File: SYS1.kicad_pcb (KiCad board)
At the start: 2 copper layers, 111 parts, among them J1 Conn_02x08_Counter_Clockwise_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, J101 Conn_01x03_Pin, J2 Micro_SD_Card, J3 SIM8051-6-0-14-01-X-REVD, J4 Conn_01x04_Pin, J5 Conn_02x08_Counter_Clockwise_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, J6 2169890001, Q1 NPN, Q2 NPN, Q3 NPN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

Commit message: Pocetak PCB dizajna
Dodao fizicke definicije ploce
Dodao rupe za montazu
Kreirao inicijalnijalni placement
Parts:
- added H1: MountingHole_Pad, MountingHole:MountingHole_3.2mm_M3_DIN965_Pad_TopBottom, F.Cu at (177.5, 73.5)
- added H2: MountingHole_Pad, MountingHole:MountingHole_3.2mm_M3_DIN965_Pad_TopBottom, F.Cu at (92.5, 63.5)
- added H3: MountingHole_Pad, MountingHole:MountingHole_3.2mm_M3_DIN965_Pad_TopBottom, F.Cu at (152.5, 63.5)
- added H4: MountingHole_Pad, MountingHole:MountingHole_3.2mm_M3_DIN965_Pad_TopBottom, F.Cu at (92.5, 123.5)
- added H5: MountingHole_Pad, MountingHole:MountingHole_3.2mm_M3_DIN965_Pad_TopBottom, F.Cu at (152.5, 123.5)
- J1, J5: footprint Connector_Molex:Molex_Micro-Fit_3.0_43045-1621_2x08-1MP_P3.00mm_Horizontal -> Connector_FFC-FPC:Hirose_FH12-16S-0.5SH_1x16-1MP_P0.50mm_Horizontal
- JP101, JP102, U1, U3: moved to B.Cu
- moved C217 255.7 mm to (-49.4, 102.8)
- moved C218 255.7 mm to (-49.4, 106.2)
- moved C219 255.7 mm to (-49.4, 109.5)
- moved C220 255.7 mm to (-49.4, 112.9)
- moved C221 255.7 mm to (-49.4, 116.2)
- moved C222 255.7 mm to (-49.4, 119.6)
- moved C223 255.7 mm to (-49.4, 122.9)
- moved C224 255.7 mm to (-49.4, 126.3)
- moved R209 255.7 mm to (-76.5, 102.8)
- moved R210 255.7 mm to (-76.5, 106.1)
- moved R211 255.7 mm to (-76.5, 109.4)
- moved R212 255.7 mm to (-76.5, 112.7)
- moved R213 255.7 mm to (-76.5, 116.0)
- moved R214 255.7 mm to (-76.5, 119.3)
- moved R215 255.7 mm to (-76.5, 122.7)
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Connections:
- J1 pad 15: VDDA -> +3.3V
- J5 pad 15: VDDA -> +3.3V
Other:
- board outline added: 105 x 70 mm

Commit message: manje izmene pcb layouta
dodao konektor za napajanje
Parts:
- added J7: 430450800, 430450800:MOLEX_430450800, F.Cu at (110.2, 67.5)
- added TP1: TestPoint, TestPoint:TestPoint_Pad_D1.0mm, F.Cu at (-55.9, 38.3)
- added TP10: TestPoint, TestPoint:TestPoint_Pad_D1.0mm, F.Cu at (-52.9, 44.4)
- added TP11: TestPoint, TestPoint:TestPoint_Pad_D1.0mm, F.Cu at (-52.9, 47.5)
- added TP12: TestPoint, TestPoint:TestPoint_Pad_D1.0mm, F.Cu at (-52.9, 50.5)
- added TP13: TestPoint, TestPoint:TestPoint_Pad_D1.0mm, F.Cu at (-52.9, 53.6)
- added TP14: TestPoint, TestPoint:TestPoint_Pad_D1.0mm, F.Cu at (-52.9, 56.6)
- added TP15: TestPoint, TestPoint:TestPoint_Pad_D1.0mm, F.Cu at (-49.8, 38.3)
- added TP16: TestPoint, TestPoint:TestPoint_Pad_D1.0mm, F.Cu at (-49.8, 41.4)
- added TP17: TestPoint, TestPoint:TestPoint_Pad_D1.0mm, F.Cu at (-49.8, 44.4)
- added TP18: TestPoint, TestPoint:TestPoint_Pad_D1.0mm, F.Cu at (-49.8, 47.5)
- added TP19: TestPoint, TestPoint:TestPoint_Pad_D1.0mm, F.Cu at (-49.8, 50.5)
- added TP2: TestPoint, TestPoint:TestPoint_Pad_D1.0mm, F.Cu at (-55.9, 41.4)
- added TP20: TestPoint, TestPoint:TestPoint_Pad_D1.0mm, F.Cu at (-49.8, 53.6)
- added TP21: TestPoint, TestPoint:TestPoint_Pad_D1.0mm, F.Cu at (-49.8, 56.6)
- added TP22: TestPoint, TestPoint:TestPoint_Pad_D1.0mm, F.Cu at (-46.8, 38.3)
- added TP23: TestPoint, TestPoint:TestPoint_Pad_D1.0mm, F.Cu at (-46.8, 41.4)
- added TP24: TestPoint, TestPoint:TestPoint_Pad_D1.0mm, F.Cu at (-46.8, 44.4)
- added TP25: TestPoint, TestPoint:TestPoint_Pad_D1.0mm, F.Cu at (-46.8, 47.5)
- added TP26: TestPoint, TestPoint:TestPoint_Pad_D1.0mm, F.Cu at (-46.8, 50.5)
- added TP27: TestPoint, TestPoint:TestPoint_Pad_D1.0mm, F.Cu at (-46.8, 53.6)
- added TP28: TestPoint, TestPoint:TestPoint_Pad_D1.0mm, F.Cu at (-46.8, 56.6)
- added TP29: TestPoint, TestPoint:TestPoint_Pad_D1.0mm, F.Cu at (-43.7, 38.3)
- added TP3: TestPoint, TestPoint:TestPoint_Pad_D1.0mm, F.Cu at (-55.9, 44.4)
- added TP30: TestPoint, TestPoint:TestPoint_Pad_D1.0mm, F.Cu at (-43.7, 41.4)
- added TP31: TestPoint, TestPoint:TestPoint_Pad_D1.0mm, F.Cu at (-43.7, 44.4)
- added TP32: TestPoint, TestPoint:TestPoint_Pad_D1.0mm, F.Cu at (-43.7, 47.5)
- added TP33: TestPoint, TestPoint:TestPoint_Pad_D1.0mm, F.Cu at (-43.7, 50.5)
- added TP4: TestPoint, TestPoint:TestPoint_Pad_D1.0mm, F.Cu at (-55.9, 47.5)
- added TP5: TestPoint, TestPoint:TestPoint_Pad_D1.0mm, F.Cu at (-55.9, 50.5)
- added TP6: TestPoint, TestPoint:TestPoint_Pad_D1.0mm, F.Cu at (-55.9, 53.6)
- added TP7: TestPoint, TestPoint:TestPoint_Pad_D1.0mm, F.Cu at (-55.9, 56.6)
- added TP8: TestPoint, TestPoint:TestPoint_Pad_D1.0mm, F.Cu at (-52.9, 38.3)
- added TP9: TestPoint, TestPoint:TestPoint_Pad_D1.0mm, F.Cu at (-52.9, 41.4)
- J3: moved to B.Cu
- moved J3 34.5 mm to (147.0, 79.5)
- moved U2 0.79 mm to (136.2, 72.2)
- renumbered H5 to H1, H1 to H5

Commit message: Znacajne izmene seme
Dodao prikljucak za UV senzor
Dodao reset za GPS
Dodao ext_ant za GPS
Dodao 3D modele
Dodao testpoint-e
Sredio semu malo
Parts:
- added C307: 0, Capacitor_SMD:C_1206_3216Metric_Pad1.33x1.80mm_HandSolder, F.Cu at (51.8, 77.9)
- added C308: 0, Capacitor_SMD:C_1206_3216Metric_Pad1.33x1.80mm_HandSolder, F.Cu at (51.8, 81.2)
- added C309: 100p, Capacitor_SMD:C_1206_3216Metric_Pad1.33x1.80mm_HandSolder, F.Cu at (51.8, 84.6)
- added J302: ~, Connector_Coaxial:SMA_Amphenol_132134-16_Vertical, F.Cu at (143.2, 107.2)
- added J8: ~, Connector_Coaxial:SMA_Amphenol_132134-16_Vertical, F.Cu at (125.2, 91.0)
- added Q5: NPN, Package_TO_SOT_SMD:TSOT-23_HandSoldering, B.Cu at (145.2, 87.5)
- added R307: 0, Resistor_SMD:R_1206_3216Metric_Pad1.30x1.75mm_HandSolder, F.Cu at (45.8, 77.9)
- added R308: 0, Resistor_SMD:R_1206_3216Metric_Pad1.30x1.75mm_HandSolder, F.Cu at (45.8, 81.2)
- added R309: 1K, Resistor_SMD:R_1206_3216Metric_Pad1.30x1.75mm_HandSolder, F.Cu at (45.8, 84.5)
- added R310: 1K, Resistor_SMD:R_1206_3216Metric_Pad1.30x1.75mm_HandSolder, F.Cu at (45.8, 87.8)
- moved J101 30.1 mm to (124.5, 119.5)
- moved Y101 6.31 mm to (134.5, 93.6), turned to 90 degrees
- moved Y102 1.96 mm to (144.8, 114.2), turned to 180 degrees
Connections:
- U1 pad 23: unconnected-(U1-PA0-Pad23) -> UV
- U1 pad 67: unconnected-(U1-PA8-Pad67) -> GPS_RESET
- U302 pad 16: unconnected-(U302-RF_OUT-Pad16) -> GPS_RFOUT
- U302 pad 17: unconnected-(U302-RF_IN-Pad17) -> GPS_RFIN
- U302 pad 23: +3.3V -> Net-(Q5-C)

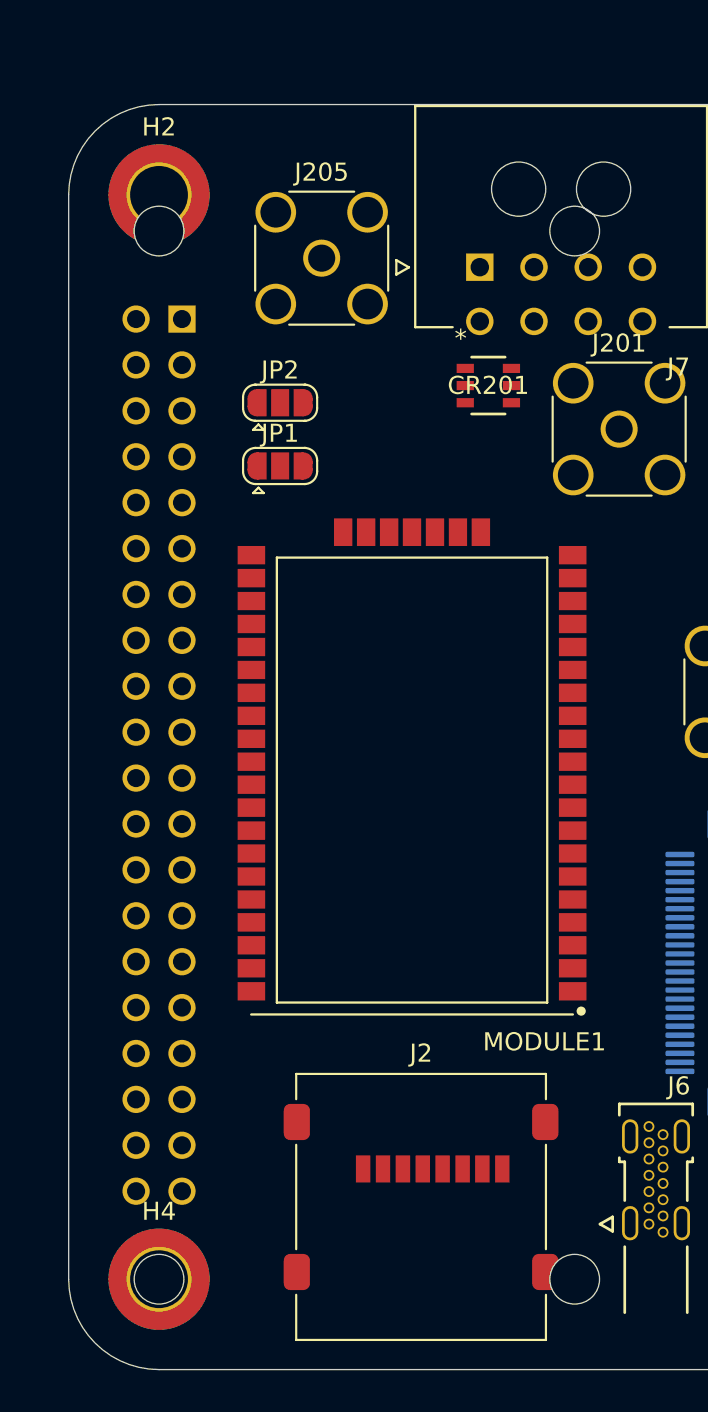
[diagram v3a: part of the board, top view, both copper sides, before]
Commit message: H2 se pomerio i izmenio RPI footprint
Pomerio mountng hole H2 da se poracna sa mounting hole na rpi
Nova pozicija je 5mm od leve ivice 7mm od gornje
Izmenio sam footprint za rpi da uklonim 2 rupe koje se nalaze na desnoj ivici zato sto nam nisu potrebne
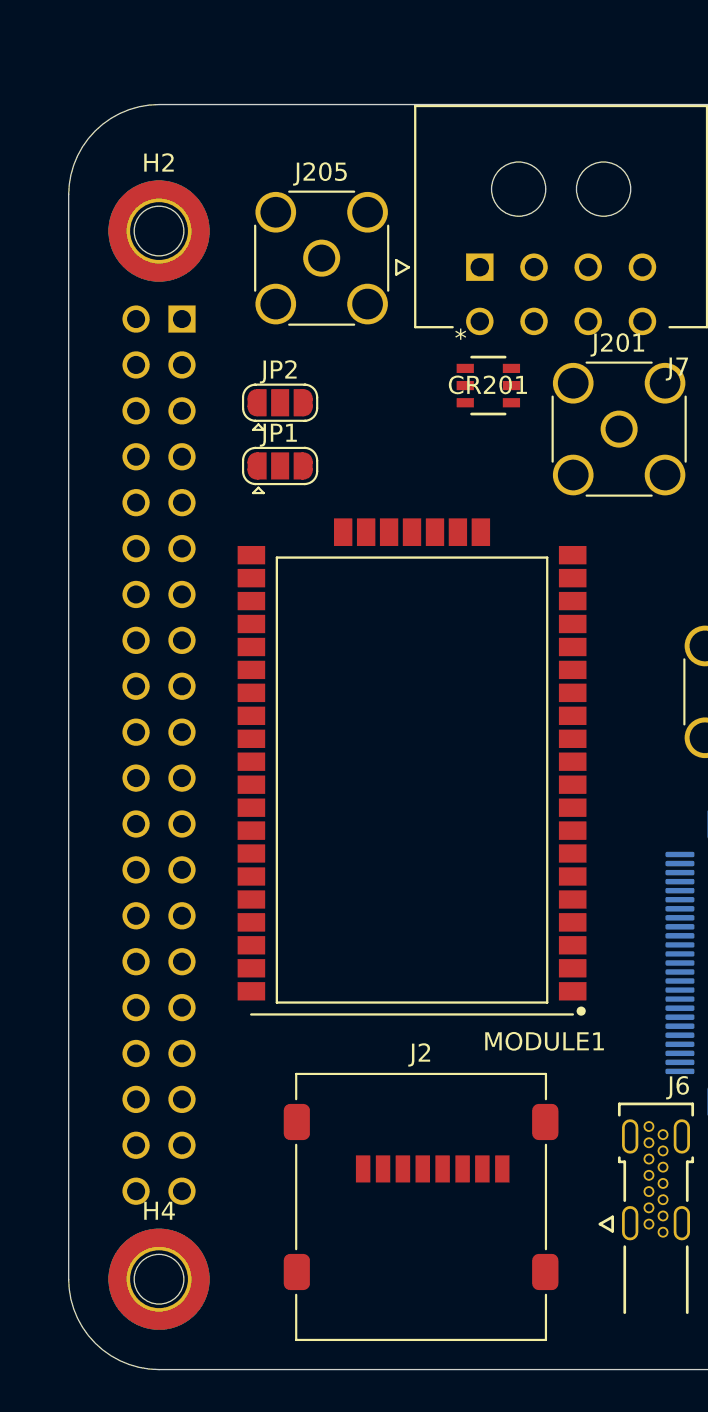
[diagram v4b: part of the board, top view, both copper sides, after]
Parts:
- moved H2 2.00 mm to (92.5, 65.5)
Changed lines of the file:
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@@
 	(footprint "MountingHole:MountingHole_3.2mm_M3_DIN965_Pad_TopBottom"
 		(layer "F.Cu")
-		(at 92.5 63.5)
+		(at 92.5 65.5)
 		(descr "Mounting Hole 3.2mm, M3, generated by kicad-footprint-generator mountinghole.py")
 		(tags "mountinghole M3 DIN965")
@@
 		)
 		(pad "" np_thru_hole circle
-			(at -29 -11.5 270)
-			(size 2.75 2.75)
-			(drill 2.75)
-			(layers "*.Cu" "*.Mask")
-		)
-		(pad "" np_thru_hole circle
 			(at -29 11.5 270)
 			(size 2.75 2.75)
 			(drill 2.75)
-			(layers "*.Cu" "*.Mask")
-		)
-		(pad "" np_thru_hole circle
-			(at 29 -11.5 270)
-			(size 2.75 2.75)
-			(drill 2.75)

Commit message: Manje izmene PCB
Podesio plocu da bude 4 sloja
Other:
- copper layers 2 -> 4
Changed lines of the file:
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@@
 	(layers
 		(0 "F.Cu" signal)
+		(4 "In1.Cu" signal)
+		(6 "In2.Cu" signal)
 		(2 "B.Cu" signal)
 		(9 "F.Adhes" user "F.Adhesive")
@@
 	)
 	(setup
+		(stackup
+			(layer "F.SilkS"
+				(type "Top Silk Screen")
+			)
+			(layer "F.Paste"
+				(type "Top Solder Paste")
+			)
+			(layer "F.Mask"
+				(type "Top Solder Mask")
+				(thickness 0.01)
+			)
+			(layer "F.Cu"
+				(type "copper")
+				(thickness 0.035)
+			)
+			(layer "dielectric 1"
+				(type "prepreg")
+				(thickness 0.1)
+				(material "FR4")
+				(epsilon_r 4.5)
+				(loss_tangent 0.02)
+			)
+			(layer "In1.Cu"
+				(type "copper")
+				(thickness 0.035)
+			)
+			(layer "dielectric 2"
+				(type "core")
+				(thickness 1.24)
+				(material "FR4")
+				(epsilon_r 4.5)
+				(loss_tangent 0.02)
+			)
+			(layer "In2.Cu"
+				(type "copper")
+				(thickness 0.035)
+			)
+			(layer "dielectric 3"
+				(type "prepreg")
+				(thickness 0.1)
+				(material "FR4")
+				(epsilon_r 4.5)
+				(loss_tangent 0.02)
+			)
+			(layer "B.Cu"
+				(type "copper")
+				(thickness 0.035)
+			)
+			(layer "B.Mask"
+				(type "Bottom Solder Mask")
+				(thickness 0.01)
+			)
+			(layer "B.Paste"
+				(type "Bottom Solder Paste")
+			)
+			(layer "B.SilkS"
+				(type "Bottom Silk Screen")
+			)
+			(copper_finish "None")
+			(dielectric_constraints no)
+		)
 		(pad_to_mask_clearance 0)
 		(allow_soldermask_bridges_in_footprints no)

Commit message: Layout i rutiranje za EXT PCB uradjeni
Uradio sam layout i rutiranje za plocicu sa sijalicama i senzorom temperature koja ce biti montirana napolju
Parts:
- J2, R1, R10, R11, R2, R3, R4, R5, R6, R7, R8, R9: moved to B.Cu
- moved R11 246.8 mm to (187.5, 66.8), turned to 180 degrees
- moved R10 246.7 mm to (187.5, 64.2), turned to 180 degrees
- moved R9 246.7 mm to (187.5, 61.8), turned to 180 degrees
- moved R6 232.1 mm to (166.5, 66.8)
- moved R5 231.6 mm to (166.5, 69.2)
- moved R4 231.2 mm to (166.5, 71.8)
- moved R1 231.1 mm to (166.5, 79.2)
- moved R3 231.0 mm to (166.5, 74.2)
- moved R2 231.0 mm to (166.5, 76.8)
- moved R8 225.5 mm to (166.5, 61.8)
- moved R7 225.2 mm to (166.5, 64.2)
- moved C301 197.1 mm to (189.8, 69.8)
- moved R301 192.8 mm to (189.8, 78.8), turned to -90 degrees
- moved J2 60.3 mm to (134.8, 66.0)
- moved JP301 60.1 mm to (186.8, 84.0), turned to 90 degrees
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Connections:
- C301 pad 1: +3.3V -> EXR_+3.3V
- C301 pad 2: GND -> EXT_GND
- H5 pad 1: GND -> EXT_GND
- J5 pad 15: +3.3V -> EXR_+3.3V
- J5 pad 16: GND -> EXT_GND
- J5 pad MP: GND -> EXT_GND
- JP301 pad 1: GND -> EXT_GND
- JP301 pad 3: +3.3V -> EXR_+3.3V
- R1 pad 2: GND -> EXT_GND
- R10 pad 2: GND -> EXT_GND
- R11 pad 2: GND -> EXT_GND
- R2 pad 2: GND -> EXT_GND
- R3 pad 2: GND -> EXT_GND
- R4 pad 2: GND -> EXT_GND
- R5 pad 2: GND -> EXT_GND
- R6 pad 2: GND -> EXT_GND
- R7 pad 2: GND -> EXT_GND
- R8 pad 2: GND -> EXT_GND
- R9 pad 2: GND -> EXT_GND
- U300 pad 2: GND -> EXT_GND
- U300 pad 5: +3.3V -> EXR_+3.3V
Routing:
- net EXT_GND: track 0.00 -> 96.5 mm, vias 0 -> 4
- net LORA_DIAG_EXT: track 0.00 -> 33.3 mm
- net LOG_DIAG_EXT: track 0.00 -> 31.6 mm
- net EXR_+3.3V: track 0.00 -> 27.0 mm, vias 0 -> 2
- net RPI_DIAG_EXT: track 0.00 -> 23.8 mm
- net TPM_DIAG_EXT: track 0.00 -> 21.6 mm
- net SYS2_DIAG_EXT: track 0.00 -> 21.3 mm
- net LA_EXT: track 0.00 -> 19.6 mm
- net PSU_DIAG_EXT: track 0.00 -> 18.4 mm
- net GSM_DIAG_EXT: track 0.00 -> 15.7 mm
- net I2C_SDA_EXT: track 0.00 -> 14.5 mm
- net I2C_SCL_EXT: track 0.00 -> 13.1 mm
- net GPS_DIAG_EXT: track 0.00 -> 13.0 mm
- net MS_DIAG_EXT: track 0.00 -> 10.7 mm
- net BME_DIAG_EXT: track 0.00 -> 10.6 mm
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- added copper zone on B.Cu, net EXT_GND

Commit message: Dodata baterija
Dodao pin za bateriju na konektor za napajanje
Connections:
- J7 pad 8: unconnected-(J7-Pad8) -> VBAT

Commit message: Znacajne izmene seme i pcb-a
Napravljen nov layout
dodat konektor za gpio
dodat konektor za eksterna merenja vetra
izmenjene diag lampice
izmenjen konektor za ext plocu
razno
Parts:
- removed D10, D11, D5, D6, D7, D8, D9: LED, LED_SMD:LED_1206_3216Metric_Pad1.42x1.75mm_HandSolder
- removed R10, R11, R5, R6, R7, R8, R9: 160R, Resistor_SMD:R_1206_3216Metric_Pad1.30x1.75mm_HandSolder
- added J10: 8-338069-8, KiCad2:83380698, F.Cu at (108.5, 144.0)
- added J9: 338069-8, KiCad:3380698, F.Cu at (84.3, 144.0)
- added TP34: TestPoint, TestPoint:TestPoint_Pad_D1.0mm, F.Cu at (-141.4, 76.4)
- J1: value Conn_02x08_Counter_Clockwise_MountingPin -> 338069-8; footprint Connector_FFC-FPC:Hirose_FH12-16S-0.5SH_1x16-1MP_P0.50mm_Horizontal -> KiCad:3380698
- J3, JP101, JP102, Q5, R1, R2, R3, R4, U3: moved to F.Cu
- J5: value Conn_02x08_Counter_Clockwise_MountingPin -> ~; footprint Connector_FFC-FPC:Hirose_FH12-16S-0.5SH_1x16-1MP_P0.50mm_Horizontal -> Connector_Coaxial:SMA_Amphenol_132134-16_Vertical
- JP1, JP2, JP302, JP304, Q1, Q2, R105, R106, R107, R108, R302, U301, U303: moved to B.Cu
- moved R301 365.9 mm to (-175.9, 93.0), turned to 0 degrees
- moved C301 360.4 mm to (-169.9, 93.0)
- moved U300 354.1 mm to (-164.8, 104.7), turned to 0 degrees
- moved JP301 351.0 mm to (-164.1, 93.2), turned to 0 degrees
- moved R1 342.9 mm to (-175.9, 61.2)
- moved R2 342.6 mm to (-175.9, 64.5)
- moved R3 342.5 mm to (-175.9, 67.9)
- moved R4 342.4 mm to (-175.9, 71.2)
- moved H5 323.6 mm to (-145.9, 84.5)
- moved J1 319.3 mm to (-164.0, 66.0), turned to 0 degrees
- moved D1 303.9 mm to (-136.9, 61.3)
- moved D2 303.6 mm to (-136.9, 64.7)
- moved D3 303.4 mm to (-136.9, 68.1)
- moved D4 303.3 mm to (-136.9, 71.5)
- moved Y102 269.0 mm to (-121.9, 79.2), turned to 0 degrees
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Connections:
- C301 pad 1: EXR_+3.3V -> EXT_+3.3V
- C309 pad 1: Net-(J302-Ext) -> Net-(J302-In)
- D1 pad 2: MS_DIAG_EXT -> DIAG1_EXT
- D2 pad 2: TPM_DIAG_EXT -> DIAG2_EXT
- D3 pad 2: BME_DIAG_EXT -> DIAG3_EXT
- D4 pad 2: GPS_DIAG_EXT -> DIAG4_EXT
- J1 pad 1: MS_DIAG -> DIAG1_EXT
- J1 pad 2: TPM_DIAG -> EXT_GND
- J1 pad 3: BME_DIAG -> DIAG2_EXT
- J1 pad 4: GPS_DIAG -> I2C_SDA_EXT
- J1 pad 5: GSM_DIAG -> DIAG3_EXT
- J1 pad 6: PSU_DIAG -> I2C_SCL_EXT
- J1 pad 7: SYS2_DIAG -> DIAG4_EXT
- J1 pad 8: RPI_DIAG -> EXT_+3.3V
- J302 pad 1: GND -> Net-(J302-In)
- J302 pad 2: Net-(J302-Ext) -> GND
- J5 pad 1: MS_DIAG_EXT -> Tijana/Jana_AD
- J5 pad 2: TPM_DIAG_EXT -> GND
- JP301 pad 3: EXR_+3.3V -> EXT_+3.3V
- TP30 pad 1: +3.3V -> NRST
- TP31 pad 1: +5V -> +3.3V
- TP32 pad 1: VCC -> +5V
- TP33 pad 1: GND -> VCC
- U1 pad 1: GSM_NETWORK_LED -> GPIO2
- U1 pad 2: LOC_GPS -> GPIO3
- U1 pad 24: unconnected-(U1-PA1-Pad24) -> Tijana/Jana_AD
- U1 pad 3: PPS_GPS -> GPIO4
- U1 pad 38: PSU_DIAG -> GPIO7
- U1 pad 39: SYS2_DIAG -> GPIO8
- U1 pad 4: LA -> GPIO5
- U1 pad 40: LOG_DIAG -> GPIO9
- U1 pad 41: LORA_DIAG -> GPIO10
- U1 pad 42: MS_DIAG -> GPIO11
- U1 pad 43: TPM_DIAG -> GPIO12
- U1 pad 44: BME_DIAG -> GPIO13
- U1 pad 45: GPS_DIAG -> GPIO14
- U1 pad 46: GSM_DIAG -> GPIO15
- U1 pad 5: RPI_DIAG -> GPIO6
- U1 pad 57: unconnected-(U1-PD10-Pad57) -> DIAG1
- U1 pad 58: unconnected-(U1-PD11-Pad58) -> DIAG2
- U1 pad 59: unconnected-(U1-PD12-Pad59) -> DIAG3
- U1 pad 60: unconnected-(U1-PD13-Pad60) -> DIAG4
- U1 pad 84: unconnected-(U1-PD3-Pad84) -> LORA_RESET
- U1 pad 85: unconnected-(U1-PD4-Pad85) -> PWRKEY
- U1 pad 86: unconnected-(U1-PD5-Pad86) -> GSM_NETWORK_LED
- U1 pad 87: unconnected-(U1-PD6-Pad87) -> LOC_GPS
- U1 pad 88: unconnected-(U1-PD7-Pad88) -> PPS_GPS
- U1 pad 97: LORA_RESET -> GPIO0
- U1 pad 98: PWRKEY -> GPIO1
- U300 pad 5: EXR_+3.3V -> EXT_+3.3V
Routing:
- net EXT_GND: track 96.5 -> 0.00 mm, vias 4 -> 0
- net LORA_DIAG_EXT: track 33.3 -> 0.00 mm
- net LOG_DIAG_EXT: track 31.6 -> 0.00 mm
- net EXR_+3.3V: track 27.0 -> 0.00 mm, vias 2 -> 0
- net RPI_DIAG_EXT: track 23.8 -> 0.00 mm
- net TPM_DIAG_EXT: track 21.6 -> 0.00 mm
- net SYS2_DIAG_EXT: track 21.3 -> 0.00 mm
- net LA_EXT: track 19.6 -> 0.00 mm
- net PSU_DIAG_EXT: track 18.4 -> 0.00 mm
- net GSM_DIAG_EXT: track 15.7 -> 0.00 mm
- net I2C_SDA_EXT: track 14.5 -> 0.00 mm
- net I2C_SCL_EXT: track 13.1 -> 0.00 mm
- net GPS_DIAG_EXT: track 13.0 -> 0.00 mm
- net MS_DIAG_EXT: track 10.7 -> 0.00 mm
- net BME_DIAG_EXT: track 10.6 -> 0.00 mm
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- removed copper zone on B.Cu, net EXT_GND
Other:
- board size 105 x 70 mm -> 100 x 100 mm
